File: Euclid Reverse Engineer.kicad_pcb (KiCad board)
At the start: 2 copper layers, 14.5 x 28.2 mm, 9 parts, among them J1 Conn_01x04_Female

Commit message: Added my name
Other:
- board text added: "By: Daddy G"
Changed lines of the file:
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@@
   (gr_arc (start 143.6 108.6) (mid 143.536513 108.051226) (end 143.5 107.5) (layer "Edge.Cuts") (width 0.1))
   (gr_arc (start 154.4 119.8) (mid 150.760434 122.759652) (end 147.120868 119.8) (layer "Edge.Cuts") (width 0.1))
+  (gr_text "By: Daddy G" (at 156.25 105.25 90) (layer "F.SilkS")
+    (effects (font (size 1 1) (thickness 0.15)))
+  )
   (segment (start 150.75 113.5) (end 150.75 116.8) (width 0.5) (layer "F.Cu") (net 1))
   (segment (start 153.625 113.375) (end 150.875 113.375) (width 0.5) (layer "B.Cu") (net 1))

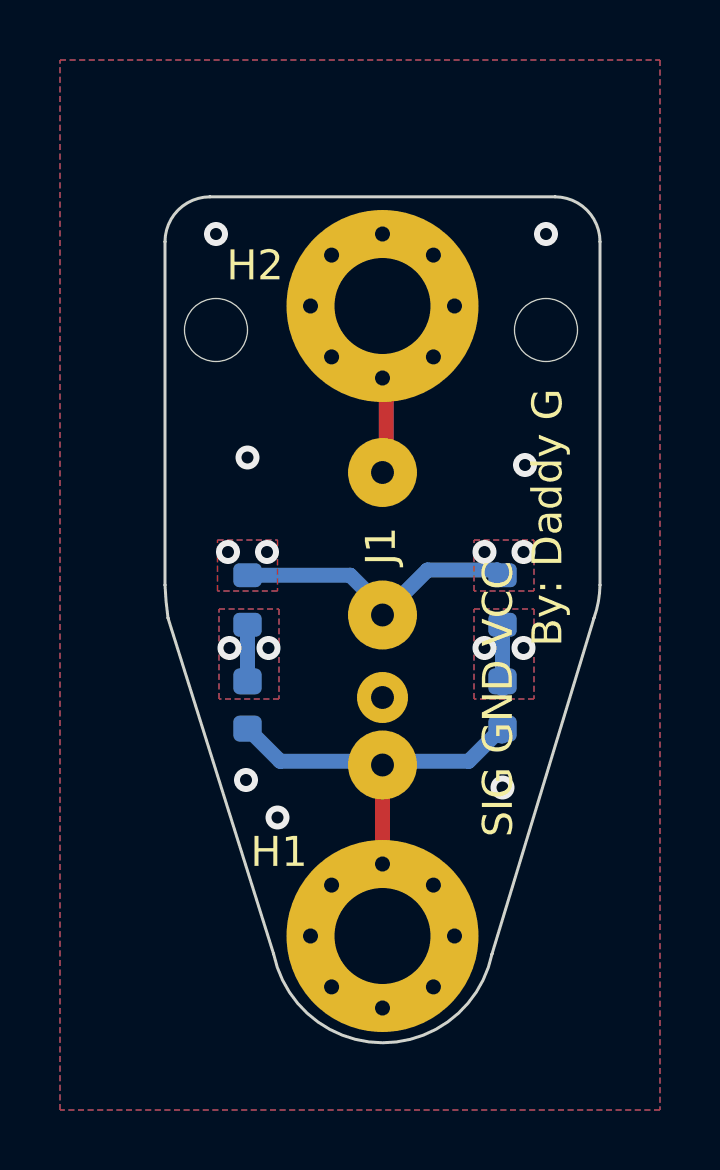
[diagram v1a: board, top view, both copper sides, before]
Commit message: Fixing sdpt spacing
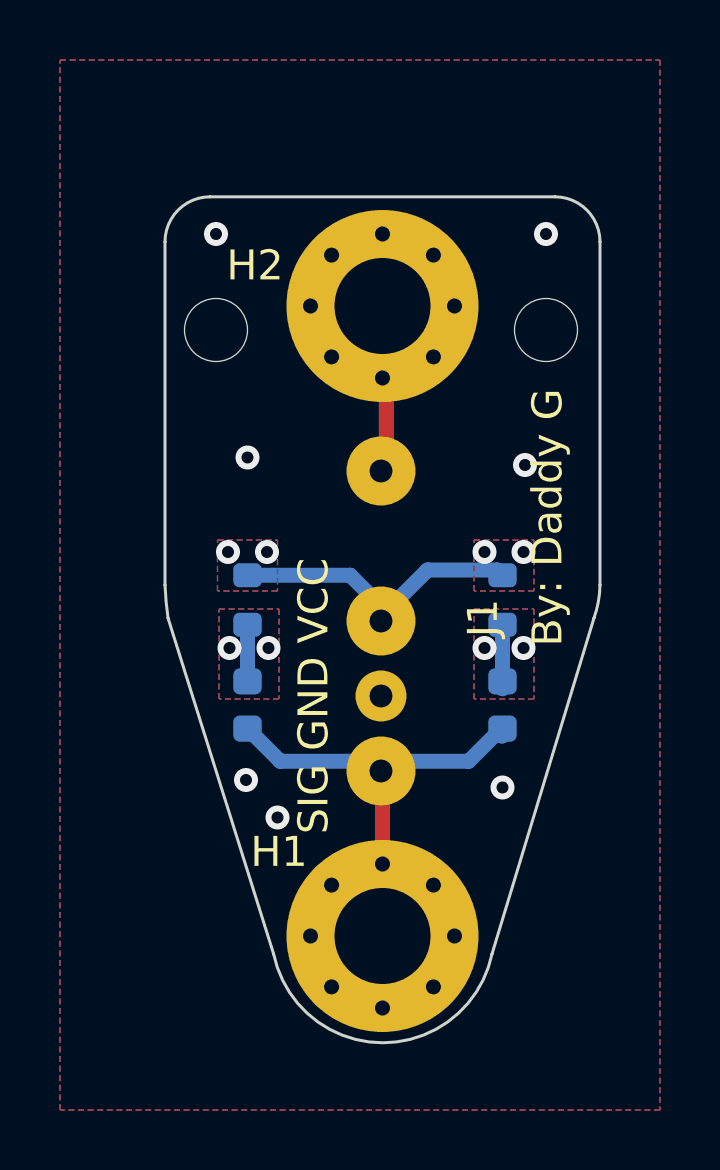
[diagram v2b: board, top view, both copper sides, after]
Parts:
- J1: value Conn_01x04_Female -> sdpt
- moved J1 0.21 mm to (150.7, 108.7)
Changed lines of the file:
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@@
   )
   (footprint "custom:sdpt" (layer "F.Cu")
-    (at 150.75 108.5 90)
+    (at 150.7 108.7 90)
     (property "Sheetfile" "Euclid Reverse Engineer.kicad_sch")
     (property "Sheetname" "")
     (attr through_hole)
-    (fp_text reference "J1" (at 2.3 -0.05 90 unlocked) (layer "F.SilkS")
+    (fp_text reference "J1" (at 0.1 3.4 90 unlocked) (layer "F.SilkS")
       (effects (font (size 1 1) (thickness 0.15)))
     )
-    (fp_text value "Conn_01x04_Female" (at 0.1 4.9 90 unlocked) (layer "F.Fab")
+    (fp_text value "sdpt" (at 0.1 4.9 90 unlocked) (layer "F.Fab")
       (effects (font (size 1 1) (thickness 0.15)))
     )
@@
       (effects (font (size 1 1) (thickness 0.15)) (justify mirror))
     )
-    (fp_text user "SIG GND VCC" (at -2.8 3.85 90 unlocked) (layer "F.SilkS")
+    (fp_text user "SIG GND VCC" (at -2.5 -2.25 90 unlocked) (layer "F.SilkS")
       (effects (font (size 1 1) (thickness 0.15)))
     )
@@
     (pad "1" thru_hole circle (at -5 0 90) (size 2.3 2.3) (drill 0.762) (layers *.Cu *.Mask)
       (net 1 "/sig") (pinfunction "Pin_1") (pintype "passive"))
-    (pad "2" thru_hole circle (at -2.75 0 90) (size 1.7 1.7) (drill 0.762) (layers *.Cu *.Mask)
+    (pad "2" thru_hole circle (at -2.5 0 90) (size 1.7 1.7) (drill 0.762) (layers *.Cu *.Mask)
       (net 2 "/gnd") (pinfunction "Pin_2") (pintype "passive"))
     (pad "3" thru_hole circle (at 0 0 90) (size 2.3 2.3) (drill 0.762) (layers *.Cu *.Mask)
       (net 3 "/vcc") (pinfunction "Pin_3") (pintype "passive"))
-    (pad "4" thru_hole circle (at 4.75 0 90) (size 2.3 2.3) (drill 0.762) (layers *.Cu *.Mask)
+    (pad "4" thru_hole circle (at 5 0 90) (size 2.3 2.3) (drill 0.762) (layers *.Cu *.Mask)
       (net 2 "/gnd") (pinfunction "Pin_4") (pintype "passive"))
   )

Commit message: comment
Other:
- board text added: "Based on Euclid probe. Why no source files?"
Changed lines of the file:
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@@
+    (effects (font (size 1 1) (thickness 0.15)))
+  )
+  (gr_text "Based on Euclid probe.\nWhy no source files?" (at 169.4 101.4) (layer "Cmts.User")
     (effects (font (size 1 1) (thickness 0.15)))
   )
